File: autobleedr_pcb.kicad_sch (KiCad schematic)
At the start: 5 parts, among them J1 Barrel_Jack

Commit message: added header pins
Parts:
- added J2: Conn_01x13_Pin, Connector_PinHeader_2.54mm:PinHeader_1x13_P2.54mm_Vertical, symbol Connector:Conn_01x13_Pin
- added J3: Conn_01x14_Pin, Connector_PinHeader_2.54mm:PinHeader_1x14_P2.54mm_Vertical, symbol Connector:Conn_01x14_Pin
- added J4: Conn_01x08_Socket, Connector_PinHeader_2.54mm:PinHeader_1x08_P2.54mm_Vertical, symbol Connector:Conn_01x08_Socket
- added J5, J6: Conn_01x05_Pin, Connector_PinHeader_2.54mm:PinHeader_1x05_P2.54mm_Vertical, symbol Connector:Conn_01x05_Pin
- J1: footprint (none) -> Connector_BarrelJack:BarrelJack_CUI_PJ-063AH_Horizontal
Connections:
- net at U2.10 (EN): now also J4.8 (Pin_8)
- net at U2.3 (DIR): now also J4.1 (Pin_1)
- net at U2.4 (STEP): now also J4.2 (Pin_2)
- net at U2.5 (MS1): now also J4.3 (Pin_3)
- net at U2.6 (MS2): now also J4.4 (Pin_4)
- net at U2.7 (DIAG): now also J4.5 (Pin_5)
- net at U2.8 (INDEX): now also J4.6 (Pin_6)
- net at U2.9 (UART): now also J4.7 (Pin_7)
- net at U4.1 (VM): now also J6.1 (Pin_1)
- net at U4.10 (IMODE): now also J5.3 (Pin_3)
- net at U4.11 (OUT2): now also J5.2 (Pin_2)
- net at U4.12 (OUT1): now also J5.1 (Pin_1)
- net at U4.3 (EN/IN1): now also J6.2 (Pin_2)
- net at U4.4 (PH/IN2): now also J6.3 (Pin_3)
- net at U4.5 (PMODE): now also J6.4 (Pin_4)
- net at U4.7 (VREF): now also J6.5 (Pin_5)
- net at U4.8 (CS): now also J5.5 (Pin_5)
- net at U4.9 (FAULT): now also J5.4 (Pin_4)
- net at U1.1 (EN): now also J2.1 (Pin_1)
- net at U1.10 (D27): now also J2.10 (Pin_10)
- net at U1.11 (D14): now also J2.11 (Pin_11)
- net at U1.12 (D12): now also J2.12 (Pin_12)
- net at U1.13 (D13): now also J2.13 (Pin_13)
- net at U1.16 (3V3): now also J3.14 (Pin_14)
- net at U1.18 (D15): now also J3.13 (Pin_13)
- net at U1.19 (D2): now also J3.12 (Pin_12)
- net at U1.2 (VP): now also J2.2 (Pin_2)
- net at U1.20 (D4): now also J3.11 (Pin_11)
- net at U1.21 (RX2): now also J3.10 (Pin_10)
- net at U1.22 (TX2): now also J3.9 (Pin_9)
- net at U1.23 (D5): now also J3.8 (Pin_8)
- net at U1.24 (D18): now also J3.7 (Pin_7)
- net at U1.25 (D19): now also J3.6 (Pin_6)
- net at U1.26 (D21): now also J3.5 (Pin_5)
- net at U1.27 (RX0): now also J3.4 (Pin_4)
- net at U1.28 (TX0): now also J3.3 (Pin_3)
- net at U1.29 (D22): now also J3.2 (Pin_2)
- net at U1.3 (VN): now also J2.3 (Pin_3)
- net at U1.30 (D23): now also J3.1 (Pin_1)
- net at U1.4 (D34): now also J2.4 (Pin_4)
- net at U1.5 (D35): now also J2.5 (Pin_5)
- net at U1.6 (D32): now also J2.6 (Pin_6)
- net at U1.7 (D33): now also J2.7 (Pin_7)
- net at U1.8 (D25): now also J2.8 (Pin_8)
- net at U1.9 (D26): now also J2.9 (Pin_9)

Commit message: finished initial PCB
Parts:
- added J7: Screw_Terminal_01x02, TerminalBlock:TerminalBlock_MaiXu_MX126-5.0-02P_1x02_P5.00mm, symbol Connector:Screw_Terminal_01x02
- added J8, J9: Conn_01x02_Pin, Connector_PinHeader_2.54mm:PinHeader_1x02_P2.54mm_Vertical, symbol Connector:Conn_01x02_Pin
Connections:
- net +12V: now also J7.1 (Pin_1)
- net +3.3V: now also J8.1 (Pin_1), J9.1 (Pin_1)
- net GND: now also J7.2 (Pin_2), J8.2 (Pin_2), J9.2 (Pin_2)
- no-connect marks 0 -> 8

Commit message: resubmit update 1
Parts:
- added J10: XT60 Connector, Connector_AMASS:AMASS_XT60PW-F_1x02_P7.20mm_Horizontal, symbol Connector:Conn_01x02_Pin
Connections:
- net +12V: now also J10.1 (Pin_1)
- net GND: now also J10.2 (Pin_2)
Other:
- moved on the sheet: J1

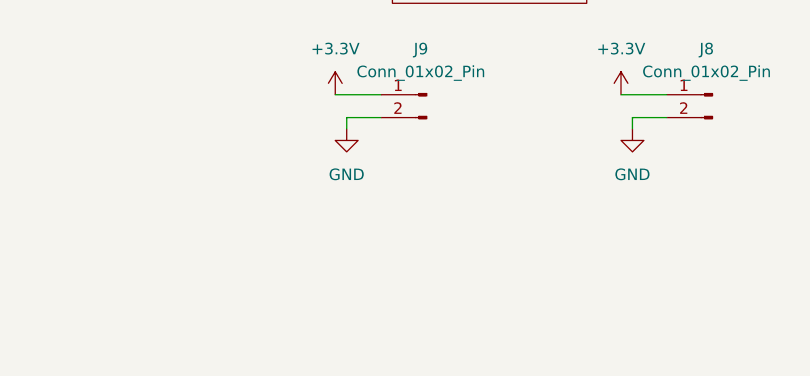
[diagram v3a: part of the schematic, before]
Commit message: Updated buck converter footprint, added stitching vias, test points, traces
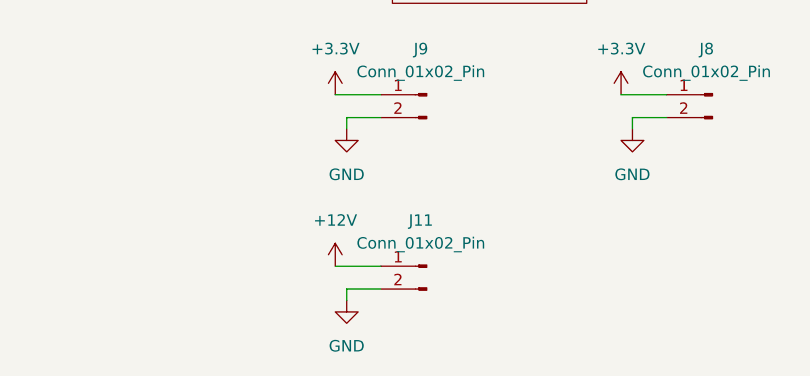
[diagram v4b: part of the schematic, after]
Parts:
- added J11: Conn_01x02_Pin, Connector_PinHeader_2.54mm:PinHeader_1x02_P2.54mm_Vertical, symbol Connector:Conn_01x02_Pin
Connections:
- net +12V: now also J11.1 (Pin_1)
- net GND: now also J11.2 (Pin_2)
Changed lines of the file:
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@@
 	(wire
 		(pts
+			(xy 151.13 129.54) (xy 154.94 129.54)
+		)
+		(stroke
+			(width 0)
+			(type default)
+		)
+	)
+	(wire
+		(pts
 			(xy 251.46 90.17) (xy 252.73 90.17)
 		)
@@
 	(wire
 		(pts
+			(xy 149.86 127) (xy 154.94 127)
+		)
+		(stroke
+			(width 0)
+			(type default)
+		)
+	)
+	(wire
+		(pts
 			(xy 181.61 107.95) (xy 186.69 107.95)
 		)
@@
 	(wire
 		(pts
+			(xy 151.13 130.81) (xy 151.13 129.54)
+		)
+		(stroke
+			(width 0)
+			(type default)
+		)
+	)
+	(wire
+		(pts
 			(xy 217.17 64.77) (xy 226.06 64.77)
 		)
@@
 	)
 	(symbol
+		(lib_id "power:GND")
+		(at 151.13 130.81 0)
+		(unit 1)
+		(exclude_from_sim no)
+		(in_bom yes)
+		(on_board yes)
+		(dnp no)
+		(fields_autoplaced yes)
+		(property "Reference" "#PWR027"
+			(at 151.13 137.16 0)
+			(effects
+				(font
+					(size 1.27 1.27)
+				)
+				(hide yes)
+			)
+		)
+		(property "Value" "GND"
+			(at 151.13 135.89 0)
+			(effects
+				(font
+					(size 1.27 1.27)
+				)
+			)
+		)
+		(property "Footprint" ""
+			(at 151.13 130.81 0)
+			(effects
+				(font
+					(size 1.27 1.27)
+				)
+				(hide yes)
+			)
+		)
+		(property "Datasheet" ""
+			(at 151.13 130.81 0)
+			(effects
+				(font
+					(size 1.27 1.27)
+				)
+				(hide yes)
+			)
+		)
+		(property "Description" "Power symbol creates a global label with name \"GND\" , ground"
+			(at 151.13 130.81 0)
+			(effects
+				(font
+					(size 1.27 1.27)
+				)
+				(hide yes)
+			)
+		)
+		(pin "1"
+		)
+		(instances
+			(project "autobleedr_pcb"
+				(path "/1cb070e6-4268-4590-be3a-70f1be021dfd"
+					(reference "#PWR027")
+					(unit 1)
+				)
+			)
+		)
+	)
+	(symbol
 		(lib_id "power:+3.3V")
 		(at 149.86 107.95 0)
@@
 	)
 	(symbol
+		(lib_id "Connector:Conn_01x02_Pin")
+		(at 160.02 127 0)
+		(mirror y)
+		(unit 1)
+		(exclude_from_sim no)
+		(in_bom yes)
+		(on_board yes)
+		(dnp no)
+		(property "Reference" "J11"
+			(at 159.385 121.92 0)
+			(effects
+				(font
+					(size 1.27 1.27)
+				)
+			)
+		)
+		(property "Value" "Conn_01x02_Pin"
+			(at 159.385 124.46 0)
+			(effects
+				(font
+					(size 1.27 1.27)
+				)
+			)
+		)
+		(property "Footprint" "Connector_PinHeader_2.54mm:PinHeader_1x02_P2.54mm_Vertical"
+			(at 160.02 127 0)
+			(effects
+				(font
+					(size 1.27 1.27)
+				)
+				(hide yes)
+			)
+		)
+		(property "Datasheet" "~"
+			(at 160.02 127 0)
+			(effects
+				(font
+					(size 1.27 1.27)
+				)
+				(hide yes)
+			)
+		)
+		(property "Description" "Generic connector, single row, 01x02, script generated"
+			(at 160.02 127 0)
+			(effects
+				(font
+					(size 1.27 1.27)
+				)
+				(hide yes)
+			)
+		)
+		(pin "2"
+		)
+		(pin "1"
+		)
+		(instances
+			(project "autobleedr_pcb"
+				(path "/1cb070e6-4268-4590-be3a-70f1be021dfd"
+					(reference "J11")
+					(unit 1)
+				)
+			)
+		)
+	)
+	(symbol
 		(lib_id "power:+3.3V")
 		(at 181.61 107.95 0)
@@
 					(unit 1)
 				)
+			)
+		)
+	)
+	(symbol
+		(lib_id "power:+12V")
+		(at 149.86 127 0)
+		(unit 1)
+		(exclude_from_sim no)
+		(in_bom yes)
+		(on_board yes)
+		(dnp no)
+		(fields_autoplaced yes)
+		(property "Reference" "#PWR026"
+			(at 149.86 130.81 0)
+			(effects
+				(font
+					(size 1.27 1.27)
+				)
+				(hide yes)
+			)
+		)
+		(property "Value" "+12V"
+			(at 149.86 121.92 0)
+			(effects
+				(font
+					(size 1.27 1.27)
+				)
+			)
+		)
+		(property "Footprint" ""
+			(at 149.86 127 0)
+			(effects
+				(font
+					(size 1.27 1.27)
+				)
+				(hide yes)
+			)
+		)
+		(property "Datasheet" ""
+			(at 149.86 127 0)
+			(effects
+				(font
+					(size 1.27 1.27)
+				)
+				(hide yes)
+			)
+		)
+		(property "Description" "Power symbol creates a global label with name \"+12V\""
+			(at 149.86 127 0)
+			(effects
+				(font
+					(size 1.27 1.27)
+				)
+				(hide yes)
+			)
+		)
+		(pin "1"
+		)
+		(instances
+			(project "autobleedr_pcb"
+				(path "/1cb070e6-4268-4590-be3a-70f1be021dfd"
+					(reference "#PWR026")
+					(unit 1)
+				)

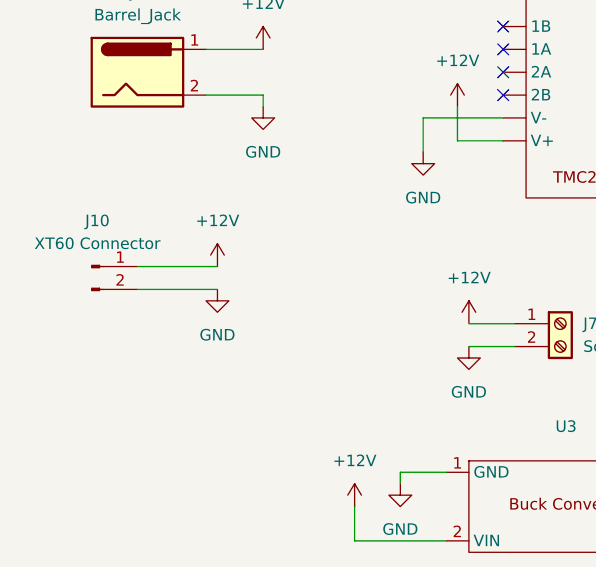
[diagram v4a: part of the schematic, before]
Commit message: finished labels, screw holes, and trace widths
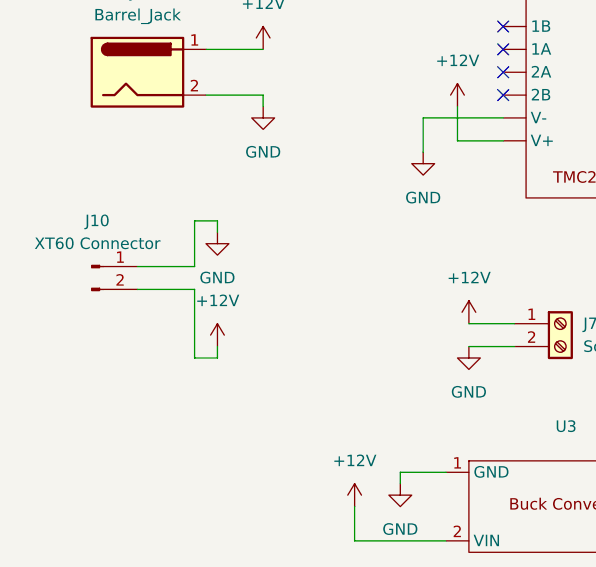
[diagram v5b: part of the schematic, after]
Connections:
- net +12V: now also J10.2 (Pin_2); no longer J10.1 (Pin_1)
- net GND: now also J10.1 (Pin_1); no longer J10.2 (Pin_2)
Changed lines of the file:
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@@
 	(wire
 		(pts
+			(xy 128.27 74.93) (xy 128.27 76.2)
+		)
+		(stroke
+			(width 0)
+			(type default)
+		)
+	)
+	(wire
+		(pts
 			(xy 251.46 90.17) (xy 252.73 90.17)
 		)
@@
 	(wire
 		(pts
+			(xy 125.73 68.58) (xy 125.73 76.2)
+		)
+		(stroke
+			(width 0)
+			(type default)
+		)
+	)
+	(wire
+		(pts
 			(xy 217.17 39.37) (xy 226.06 39.37)
 		)
@@
 	(wire
 		(pts
+			(xy 128.27 60.96) (xy 128.27 62.23)
+		)
+		(stroke
+			(width 0)
+			(type default)
+		)
+	)
+	(wire
+		(pts
 			(xy 217.17 64.77) (xy 217.17 66.04)
 		)
@@
 	(wire
 		(pts
+			(xy 125.73 66.04) (xy 125.73 60.96)
+		)
+		(stroke
+			(width 0)
+			(type default)
+		)
+	)
+	(wire
+		(pts
 			(xy 251.46 31.75) (xy 261.62 31.75)
 		)
@@
 	(wire
 		(pts
-			(xy 119.38 68.58) (xy 128.27 68.58)
+			(xy 125.73 76.2) (xy 128.27 76.2)
 		)
 		(stroke
@@
 	(wire
 		(pts
+			(xy 125.73 60.96) (xy 128.27 60.96)
+		)
+		(stroke
+			(width 0)
+			(type default)
+		)
+	)
+	(wire
+		(pts
 			(xy 251.46 67.31) (xy 261.62 67.31)
 		)
@@
 	(wire
 		(pts
+			(xy 119.38 66.04) (xy 125.73 66.04)
+		)
+		(stroke
+			(width 0)
+			(type default)
+		)
+	)
+	(wire
+		(pts
 			(xy 185.42 41.91) (xy 187.96 41.91)
 		)
@@
 	(wire
 		(pts
-			(xy 227.33 95.25) (xy 229.87 95.25)
+			(xy 119.38 68.58) (xy 125.73 68.58)
 		)
 		(stroke
@@
 	(wire
 		(pts
-			(xy 151.13 130.81) (xy 151.13 129.54)
+			(xy 227.33 95.25) (xy 229.87 95.25)
 		)
 		(stroke
@@
 	(wire
 		(pts
-			(xy 217.17 64.77) (xy 226.06 64.77)
+			(xy 151.13 130.81) (xy 151.13 129.54)
 		)
 		(stroke
@@
 	(wire
 		(pts
-			(xy 195.58 57.15) (xy 195.58 55.88)
+			(xy 217.17 64.77) (xy 226.06 64.77)
 		)
 		(stroke
@@
 	(wire
 		(pts
-			(xy 251.46 52.07) (xy 261.62 52.07)
+			(xy 195.58 57.15) (xy 195.58 55.88)
 		)
 		(stroke
@@
 	(wire
 		(pts
-			(xy 251.46 95.25) (xy 252.73 95.25)
+			(xy 251.46 52.07) (xy 261.62 52.07)
 		)
 		(stroke
@@
 	(wire
 		(pts
-			(xy 217.17 57.15) (xy 226.06 57.15)
+			(xy 251.46 95.25) (xy 252.73 95.25)
 		)
 		(stroke
@@
 	(wire
 		(pts
-			(xy 185.42 49.53) (xy 187.96 49.53)
+			(xy 217.17 57.15) (xy 226.06 57.15)
 		)
 		(stroke
@@
 	(wire
 		(pts
-			(xy 119.38 66.04) (xy 128.27 66.04)
+			(xy 185.42 49.53) (xy 187.96 49.53)
 		)
 		(stroke
@@
 	(symbol
 		(lib_id "power:+12V")
-		(at 128.27 66.04 0)
+		(at 128.27 74.93 0)
 		(unit 1)
 		(exclude_from_sim no)
@@
 		(fields_autoplaced yes)
 		(property "Reference" "#PWR024"
-			(at 128.27 69.85 0)
+			(at 128.27 78.74 0)
 			(effects
 				(font
@@
 		)
 		(property "Value" "+12V"
-			(at 128.27 60.96 0)
+			(at 128.27 69.85 0)
 			(effects
 				(font
@@
 		)
 		(property "Footprint" ""
-			(at 128.27 66.04 0)
+			(at 128.27 74.93 0)
 			(effects
 				(font
@@
 		)
 		(property "Datasheet" ""
-			(at 128.27 66.04 0)
+			(at 128.27 74.93 0)
 			(effects
 				(font
@@
 		)
 		(property "Description" "Power symbol creates a global label with name \"+12V\""
-			(at 128.27 66.04 0)
+			(at 128.27 74.93 0)
 			(effects
 				(font
@@
 	(symbol
 		(lib_id "power:GND")
-		(at 128.27 68.58 0)
+		(at 128.27 62.23 0)
 		(unit 1)
 		(exclude_from_sim no)
@@
 		(fields_autoplaced yes)
 		(property "Reference" "#PWR025"
-			(at 128.27 74.93 0)
+			(at 128.27 68.58 0)
 			(effects
 				(font
@@
 		)
 		(property "Value" "GND"
-			(at 128.27 73.66 0)
+			(at 128.27 67.31 0)
 			(effects
 				(font
@@
 		)
 		(property "Footprint" ""
-			(at 128.27 68.58 0)
+			(at 128.27 62.23 0)
 			(effects
 				(font
@@
 		)
 		(property "Datasheet" ""
-			(at 128.27 68.58 0)
+			(at 128.27 62.23 0)
 			(effects
 				(font
@@
 		)
 		(property "Description" "Power symbol creates a global label with name \"GND\" , ground"
-			(at 128.27 68.58 0)
+			(at 128.27 62.23 0)
 			(effects
 				(font

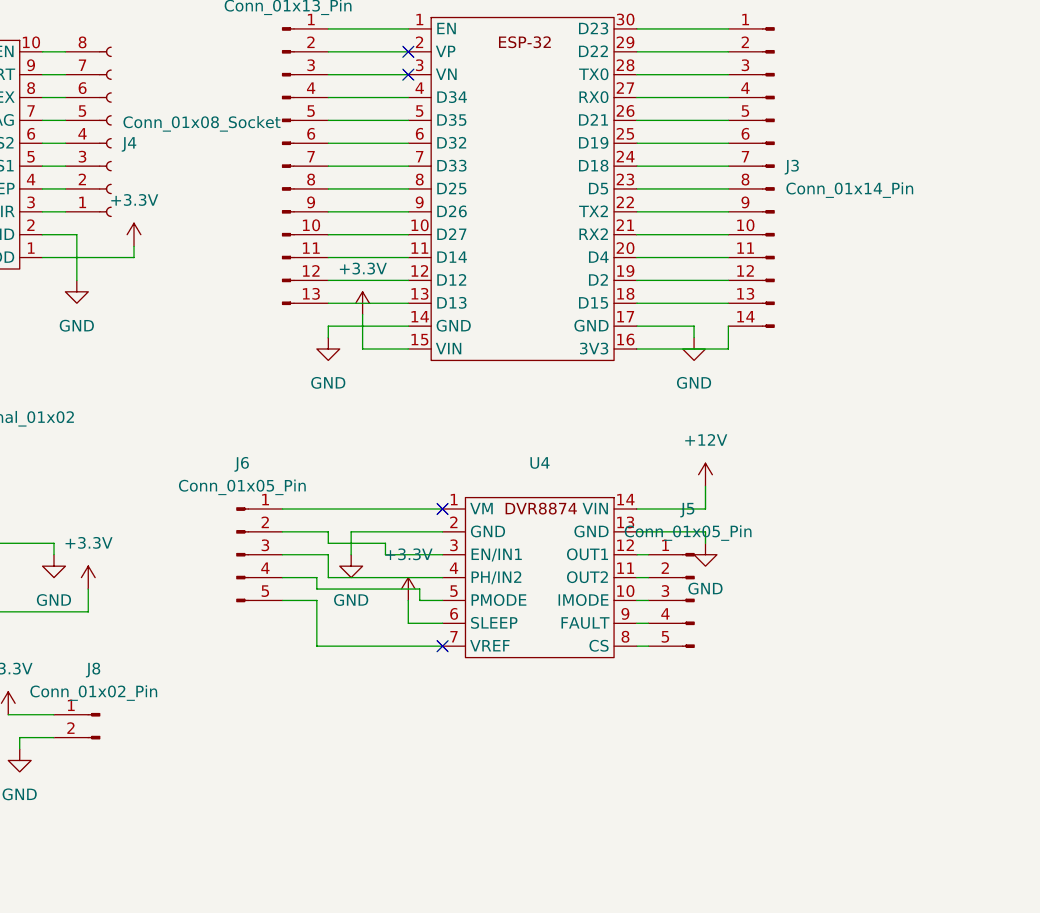
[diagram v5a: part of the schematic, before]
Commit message: updated pcb with DRV and working on compressing PCB itself:
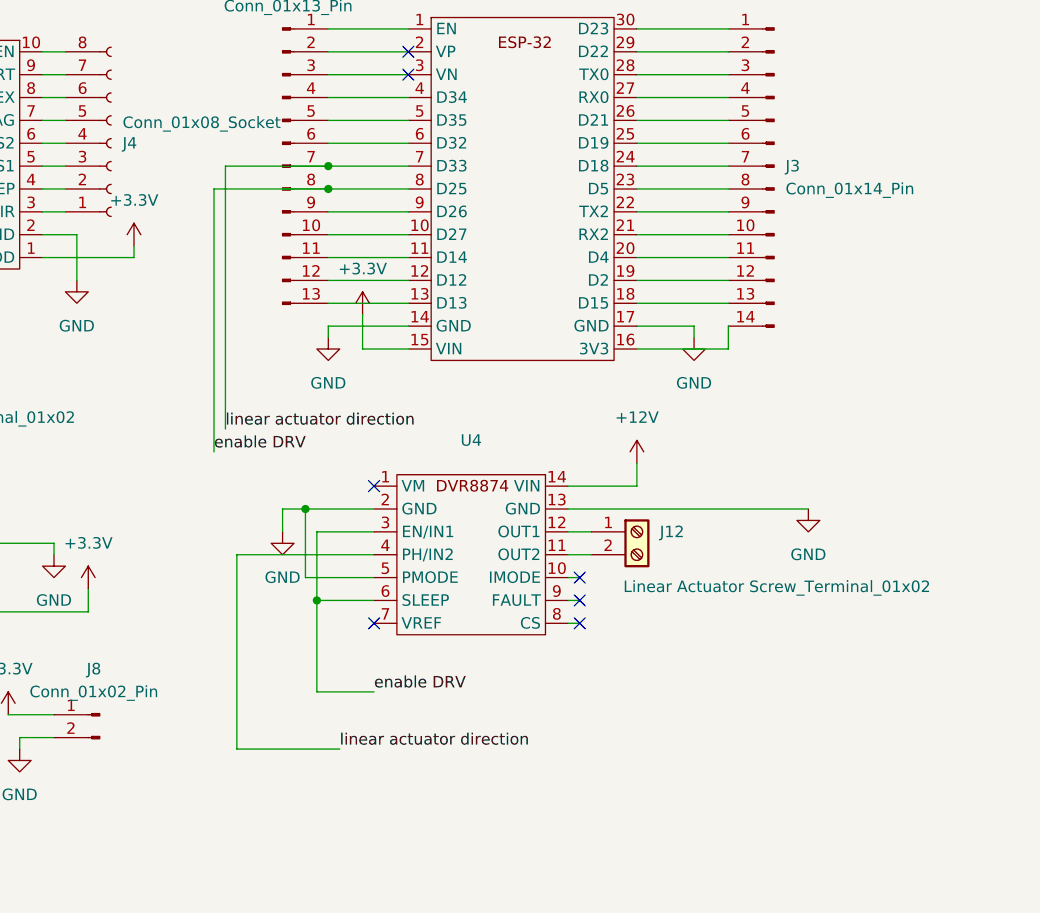
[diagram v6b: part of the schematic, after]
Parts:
- removed J5, J6: Conn_01x05_Pin, Connector_PinHeader_2.54mm:PinHeader_1x05_P2.54mm_Vertical, symbol Connector:Conn_01x05_Pin
- added J12: Linear Actuator Screw_Terminal_01x02, TerminalBlock:TerminalBlock_MaiXu_MX126-5.0-02P_1x02_P5.00mm, symbol Connector:Screw_Terminal_01x02
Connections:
- net +3.3V: no longer U4.6 (SLEEP)
- net GND: now also U4.5 (PMODE)
- net linear actuator direction: now reaches J2.7 (Pin_7), U1.7 (D33)
- net linear actuator direction: now also U4.4 (PH/IN2)
- net enable DRV: now reaches J2.8 (Pin_8), U1.8 (D25)
- net enable DRV: now also U4.3 (EN/IN1), U4.6 (SLEEP)
- net at U4.11 (OUT2): now also J12.2 (Pin_2)
- net at U4.12 (OUT1): now also J12.1 (Pin_1)
- no-connect marks 8 -> 11
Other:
- moved on the sheet: U4

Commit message: Add files via upload
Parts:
- added 0.1uF_Bypass1: C, Capacitor_THT:C_Axial_L5.1mm_D3.1mm_P7.50mm_Horizontal, symbol Device:C
- added 220_Ohm1, 330kOhm1: R, Resistor_THT:R_Axial_DIN0207_L6.3mm_D2.5mm_P7.62mm_Horizontal, symbol Device:R
- added C1: C, symbol Device:C
- added J5: IR LED, TerminalBlock:TerminalBlock_MaiXu_MX126-5.0-02P_1x02_P5.00mm, symbol Connector:Screw_Terminal_01x02
- added J6: Photo Transistor, TerminalBlock:TerminalBlock_MaiXu_MX126-5.0-02P_1x02_P5.00mm, symbol Connector:Screw_Terminal_01x02
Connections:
- net GND: now also 0.1uF_Bypass1.2, J5.1 (Pin_1), J6.1 (Pin_1)
- net D34: now reaches J2.4 (Pin_4), U1.4 (D34)
- net D34: now also 330kOhm1.2, J6.2 (Pin_2)
- net 3V3: now reaches J3.14 (Pin_14), U1.16 (3V3)
- net 3V3: now also 0.1uF_Bypass1.1, 330kOhm1.1
- net D19: now reaches J3.6 (Pin_6), U1.25 (D19)
- net D19: now also 220_Ohm1.1
- new net: 220_Ohm1.2, J5.2 (Pin_2)

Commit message: updated schematic
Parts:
- removed C1: C, symbol Device:C
- removed J12: Linear Actuator Screw_Terminal_01x02, TerminalBlock:TerminalBlock_MaiXu_MX126-5.0-02P_1x02_P5.00mm, symbol Connector:Screw_Terminal_01x02
- removed J5: IR LED, TerminalBlock:TerminalBlock_MaiXu_MX126-5.0-02P_1x02_P5.00mm, symbol Connector:Screw_Terminal_01x02
- removed J6: Photo Transistor, TerminalBlock:TerminalBlock_MaiXu_MX126-5.0-02P_1x02_P5.00mm, symbol Connector:Screw_Terminal_01x02
- added J13: Screw_Terminal_01x08, Screw_Terminal_1x8:Screw_Terminal_1x8, symbol Connector:Screw_Terminal_01x08
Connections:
- net GND: now also J13.6 (Pin_6), J13.8 (Pin_8)
- net LIN ACT VIN: now reaches U4.12 (OUT1)
- net LIN ACT VIN: now also J13.1 (Pin_1)
- net LIN ACT GND: now reaches U4.11 (OUT2)
- net LIN ACT GND: now also J13.2 (Pin_2)
- net D35: now reaches J2.5 (Pin_5), U1.5 (D35)
- net D35: now also 330kOhm1.2, J13.7 (Pin_7)
- net D32: now reaches J2.6 (Pin_6), U1.6 (D32)
- net IR LED vin: now reaches 220_Ohm1.2
- net IR LED vin: now also J13.5 (Pin_5)
- net D19: no longer names the net of J3.6 (Pin_6), U1.25 (D19)
- net D19: no longer 220_Ohm1.1
- net D34: no longer names the net of J2.4 (Pin_4), U1.4 (D34)
- net D34: no longer 330kOhm1.2
- new net 32: 220_Ohm1.1
- no-connect marks 11 -> 13
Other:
- note added: "Feel Free to use these (top is VIN, bottom is GND) -->"
- moved on the sheet: 0.1uF_Bypass1, 220_Ohm1, 330kOhm1, J1, J10, J11, J4, J7, J8, J9, U2, U3
